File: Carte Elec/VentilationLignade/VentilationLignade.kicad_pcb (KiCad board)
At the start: 2 copper layers, 83 parts, among them P1 RelaisBoard1, P10 SDCard, P11 Codeur Rotatif, P12 Teensy Bottom, P13 EndStops1, P14 Teensy_Haut, P15 EndStops2, P16 Teensy_cote, P17 Retour 12V, P18 Masse_12V, P19 12V1, P2 PUIT_CAN, P20 12V2, P21 12V_1et2, P22 Teensy_Bas, P23 Serial, P24 CHEMINEE, P25 RT_CLK1, P26 RT_CLK2, P3 RelaisBoard2, P4 TEMP_EXT, P5 RelaisBoard3, P6 TEMP_INT, P7 RelaisBoard4, P8 RelaisBoard5, P9 TFT, SW2 BackLight_On/ff, U2 OPTO-TRANSISTOR, U3 OPTO-TRANSISTOR, U4 OPTO-TRANSISTOR, U5 OPTO-TRANSISTOR, U6 OPTO-TRANSISTOR

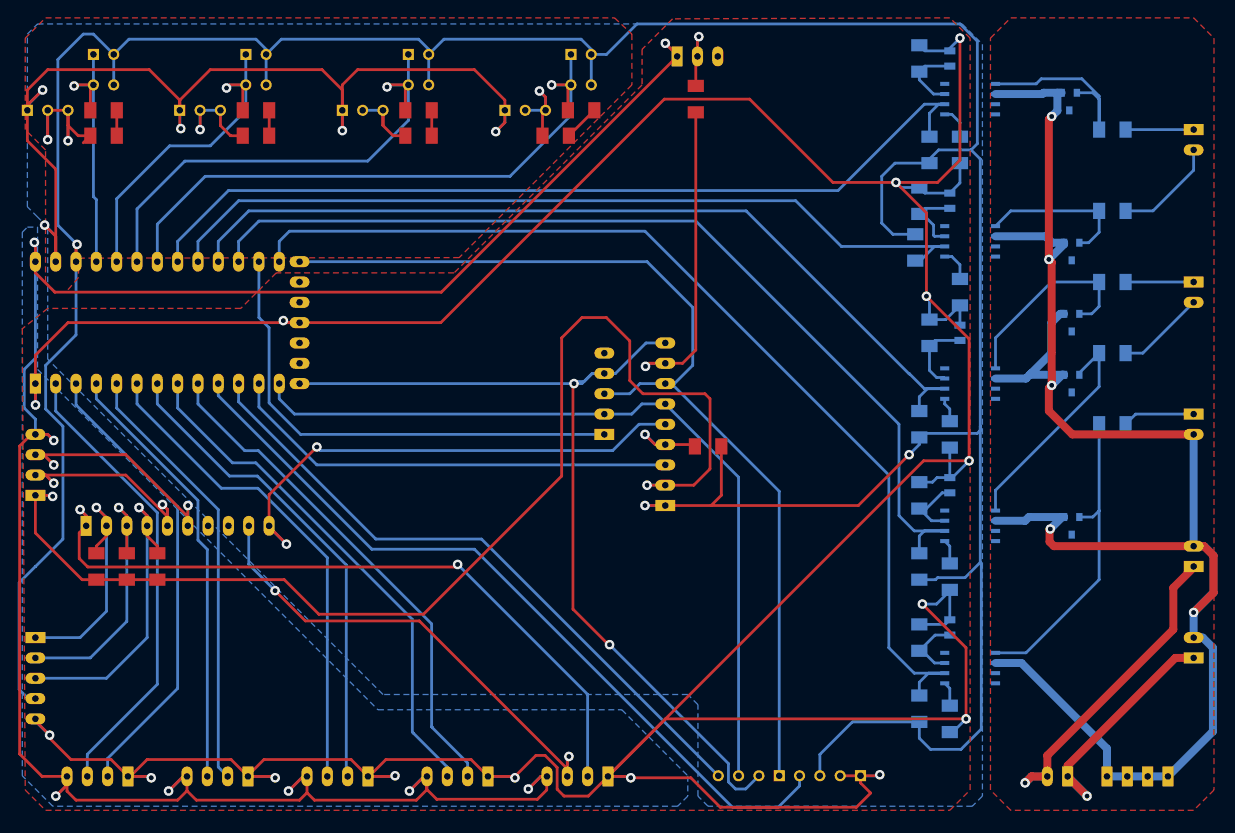
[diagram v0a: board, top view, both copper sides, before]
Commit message: Modif pour ouvrir sur Kicad last version
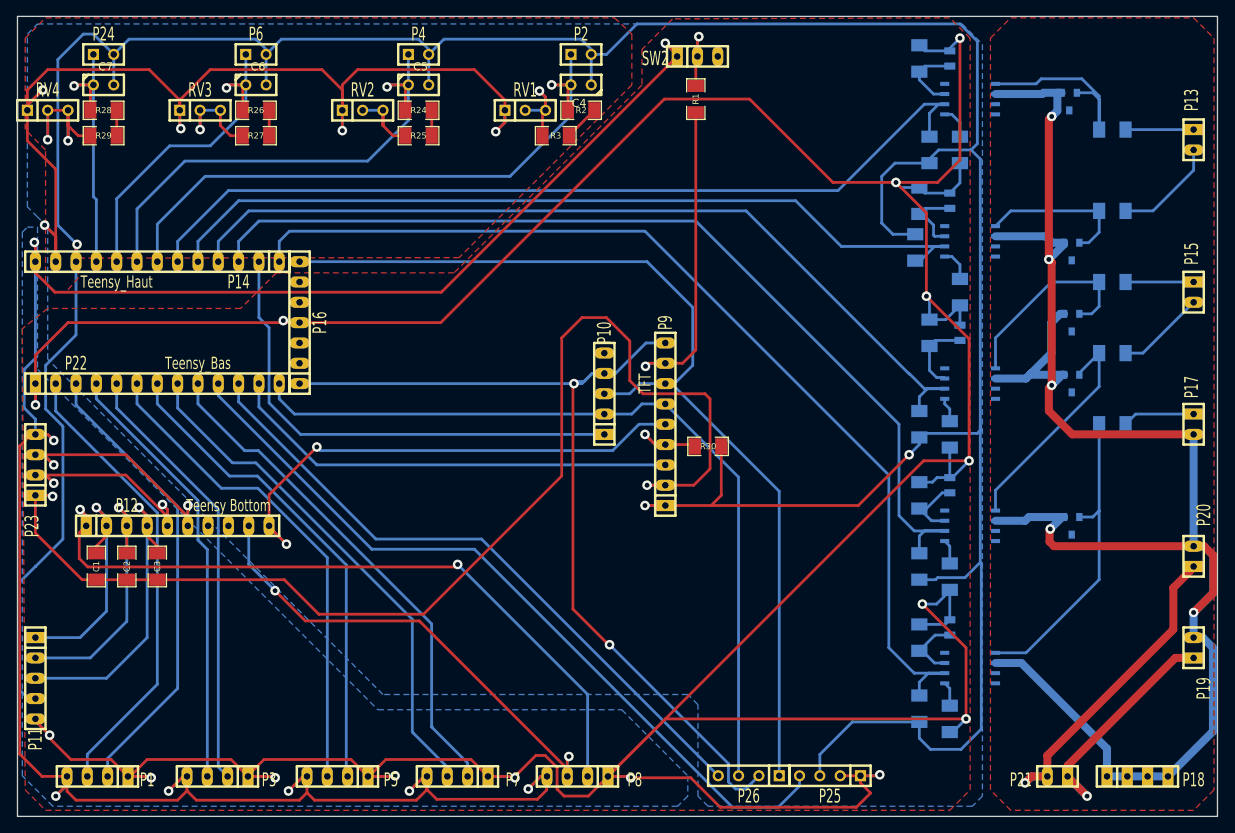
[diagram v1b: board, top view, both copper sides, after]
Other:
- board outline added: 150 x 100 mm

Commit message: Changement des boitiers en cours de reroutage
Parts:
- C4, C5, C6, C7: footprint C1 -> Capacitors_ThroughHole:C_Radial_D8_L11.5_P3.5
- P1, P18, P3, P5, P7, P8: footprint SIL-4 -> Pin_Headers:Pin_Header_Straight_1x04
- P10, P11: footprint SIL-5 -> Pin_Headers:Pin_Header_Straight_1x05
- P12: footprint SIL-10 -> Pin_Headers:Pin_Header_Straight_1x10
- P13, P15, P17, P19, P2, P20, P21, P24, P4, P6: footprint SIL-2 -> Connect:bornier2
- P14, P22: footprint SIL-13 -> Pin_Headers:Pin_Header_Straight_1x13
- P16: footprint SIL-7 -> Pin_Headers:Pin_Header_Straight_1x07
- P9: footprint SIL-9 -> Pin_Headers:Pin_Header_Straight_1x09
- R2, R24, R25, R26, R27, R28, R29, R3: footprint SM1206 -> Resistors_SMD:R_1206_HandSoldering
- RV1, RV2, RV3, RV4: footprint SIL-3 -> Potentiometers:Potentiometer_Bourns_3339S_Angular_ScrewFront
- SW2: footprint SIL-3 -> Pin_Headers:Pin_Header_Straight_1x03
- moved RV3 56.5 mm to (201.9, 105.4)
- moved C4 50.4 mm to (143.5, 115.6), turned to 0 degrees
- moved R2 45.8 mm to (148.6, 121.9)
- moved P2 45.1 mm to (148.6, 105.4), turned to 180 degrees
- moved P6 36.2 mm to (189.2, 105.4), turned to 180 degrees
- moved R27 36.2 mm to (189.2, 115.6), turned to 90 degrees
- moved R3 33.0 mm to (157.5, 115.6), turned to 90 degrees
- moved R26 29.7 mm to (181.6, 121.9)
- moved C6 27.8 mm to (180.3, 115.6)
- moved RV1 26.7 mm to (161.3, 105.4)
- moved P20 18.6 mm to (269.2, 188.0)
- moved RV2 17.3 mm to (181.6, 105.4)
- moved RV4 16.2 mm to (141.0, 105.4)
- moved P22 15.5 mm to (125.2, 147.8), turned to 90 degrees
- moved P14 15.0 mm to (155.7, 132.6), turned to 270 degrees
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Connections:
- C4 pad 1: +3.3V -> TPUIT_AN
- C4 pad 2: TPUIT_AN -> +3.3V
- P10 pad 5: (no net) -> Net-(P10-Pad5)
- P12 pad 7: (no net) -> Net-(P12-Pad7)
- P12 pad 8: (no net) -> Net-(P12-Pad8)
- P13 pad 1: /Optocouplers/END_1_1 -> /Optocouplers/END_1_2
- P13 pad 2: /Optocouplers/END_1_2 -> /Optocouplers/END_1_1
- P14 pad 7: TPUIT_AN -> TINT_AN
- P14 pad 9: TINT_AN -> TPUIT_AN
- P15 pad 1: /Optocouplers/END_2_1 -> /Optocouplers/END_2_2
- P15 pad 2: /Optocouplers/END_2_2 -> /Optocouplers/END_2_1
- P16 pad 2: (no net) -> Net-(P16-Pad2)
- P16 pad 3: (no net) -> Net-(P16-Pad3)
- P16 pad 5: (no net) -> Net-(P16-Pad5)
- P16 pad 6: (no net) -> Net-(P16-Pad6)
- P17 pad 1: /Optocouplers/12V_IN -> GNDPWR
- P17 pad 2: GNDPWR -> /Optocouplers/12V_IN
- P2 pad 1: TPUIT_AN -> +3.3V
- P2 pad 2: +3.3V -> TPUIT_AN
- P24 pad 1: TCHEM_AN -> +3.3V
- P24 pad 2: +3.3V -> TCHEM_AN
- P4 pad 1: TEXT_AN -> +3.3V
- P4 pad 2: +3.3V -> TEXT_AN
- P6 pad 1: TINT_AN -> +3.3V
- P6 pad 2: +3.3V -> TINT_AN
- SW2 pad 3: (no net) -> Net-(SW2-Pad3)
- U2 pad 3: (no net) -> Net-(U2-Pad3)
- U3 pad 3: (no net) -> Net-(U3-Pad3)
- U4 pad 3: (no net) -> Net-(U4-Pad3)
- U5 pad 3: (no net) -> Net-(U5-Pad3)
- U6 pad 3: (no net) -> Net-(U6-Pad3)
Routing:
- net TPUIT_AN: track 77.8 -> 36.7 mm, vias 1 -> 0
- net +3.3V: track 435.3 -> 395.9 mm
- net 12V2: track 40.0 -> 20.9 mm, vias 1 -> 0
- net TINT_AN: track 44.0 -> 62.9 mm, vias 1 -> 0
- net AGND: track 132.8 -> 115.1 mm, vias 5 -> 1
- net GNDPWR: track 221.9 -> 238.3 mm
- net Net-(R29-Pad2): track 24.0 -> 9.21 mm, vias 2 -> 0
- net TEXT_AN: track 62.2 -> 52.0 mm, vias 1 -> 0
- net /Optocouplers/END_1_2: track 13.2 -> 8.24 mm
- net Net-(R24-Pad2): track 3.17 -> 7.42 mm
- net Net-(R26-Pad2): track 3.17 -> 7.42 mm
- net Net-(R2-Pad2): track 4.49 -> 8.69 mm
- net 12V1: track 29.6 -> 33.6 mm, vias 1 -> 0
- net TCHEM_AN: track 34.3 -> 30.5 mm, vias 1 -> 0
- net Net-(R27-Pad2): track 12.6 -> 16.2 mm, vias 1 -> 0
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
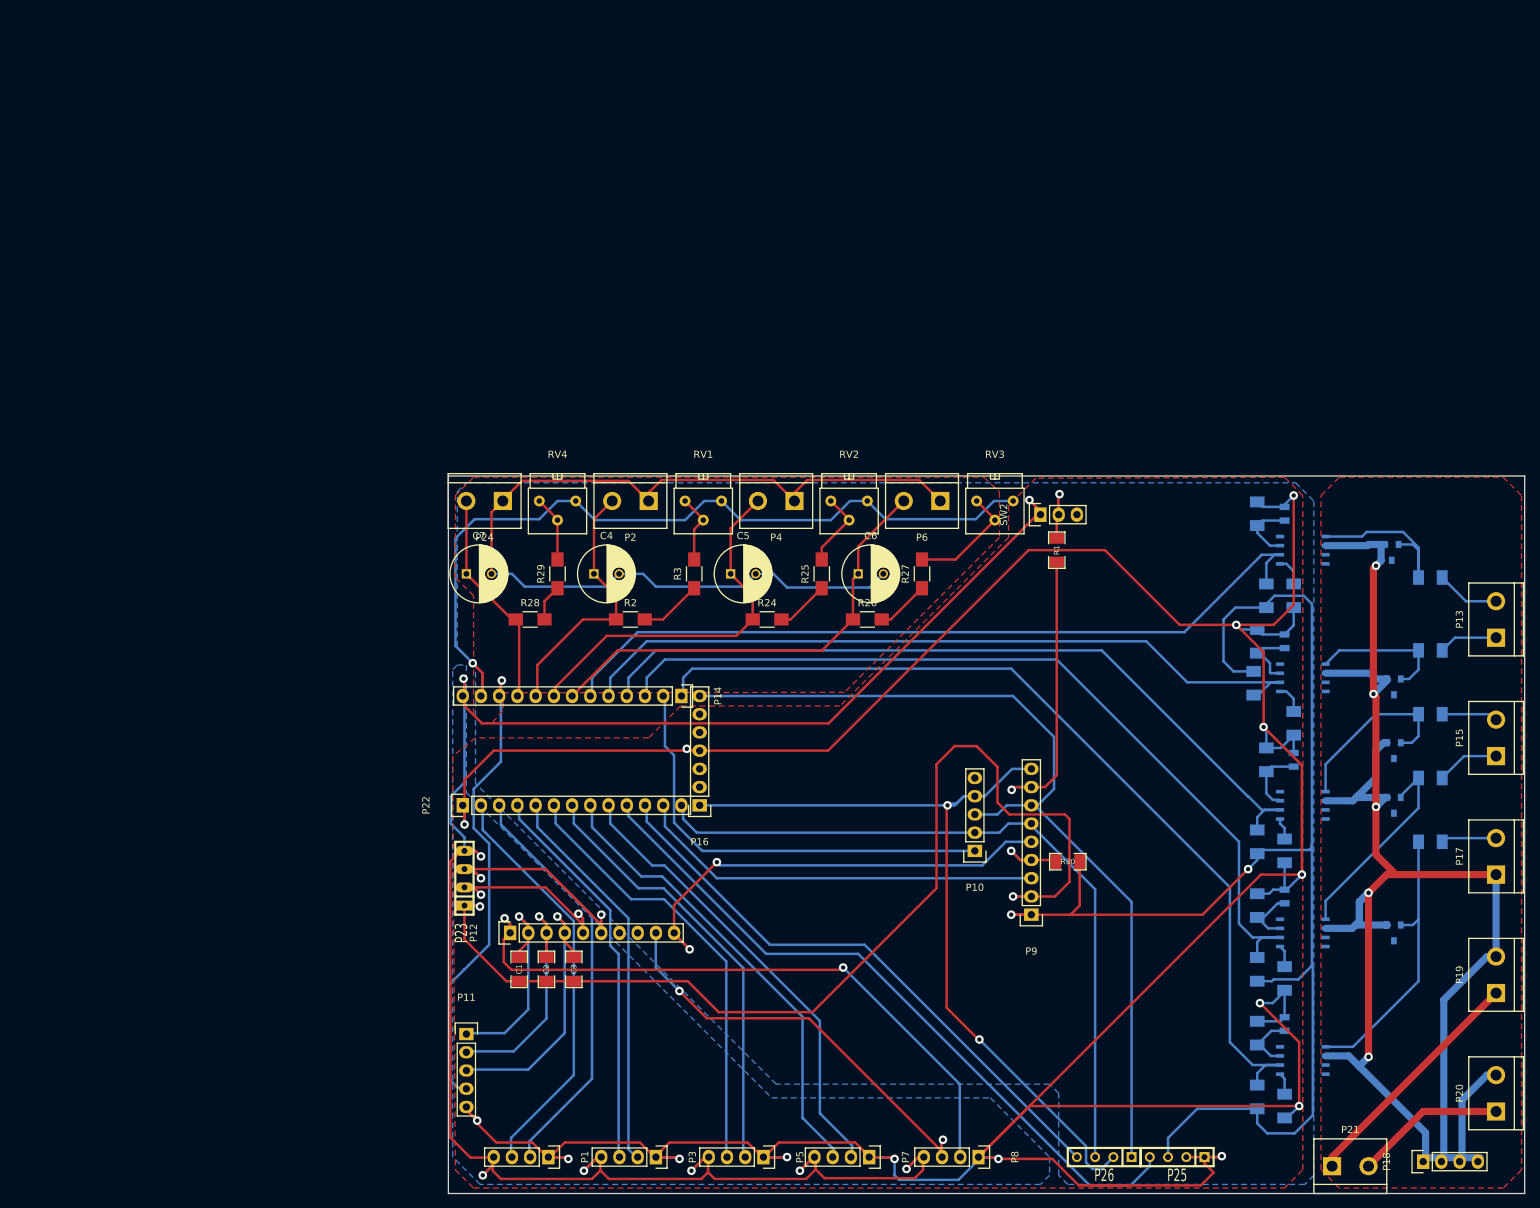
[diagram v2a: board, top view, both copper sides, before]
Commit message: Modif de la carte => Commande SEEED !!!
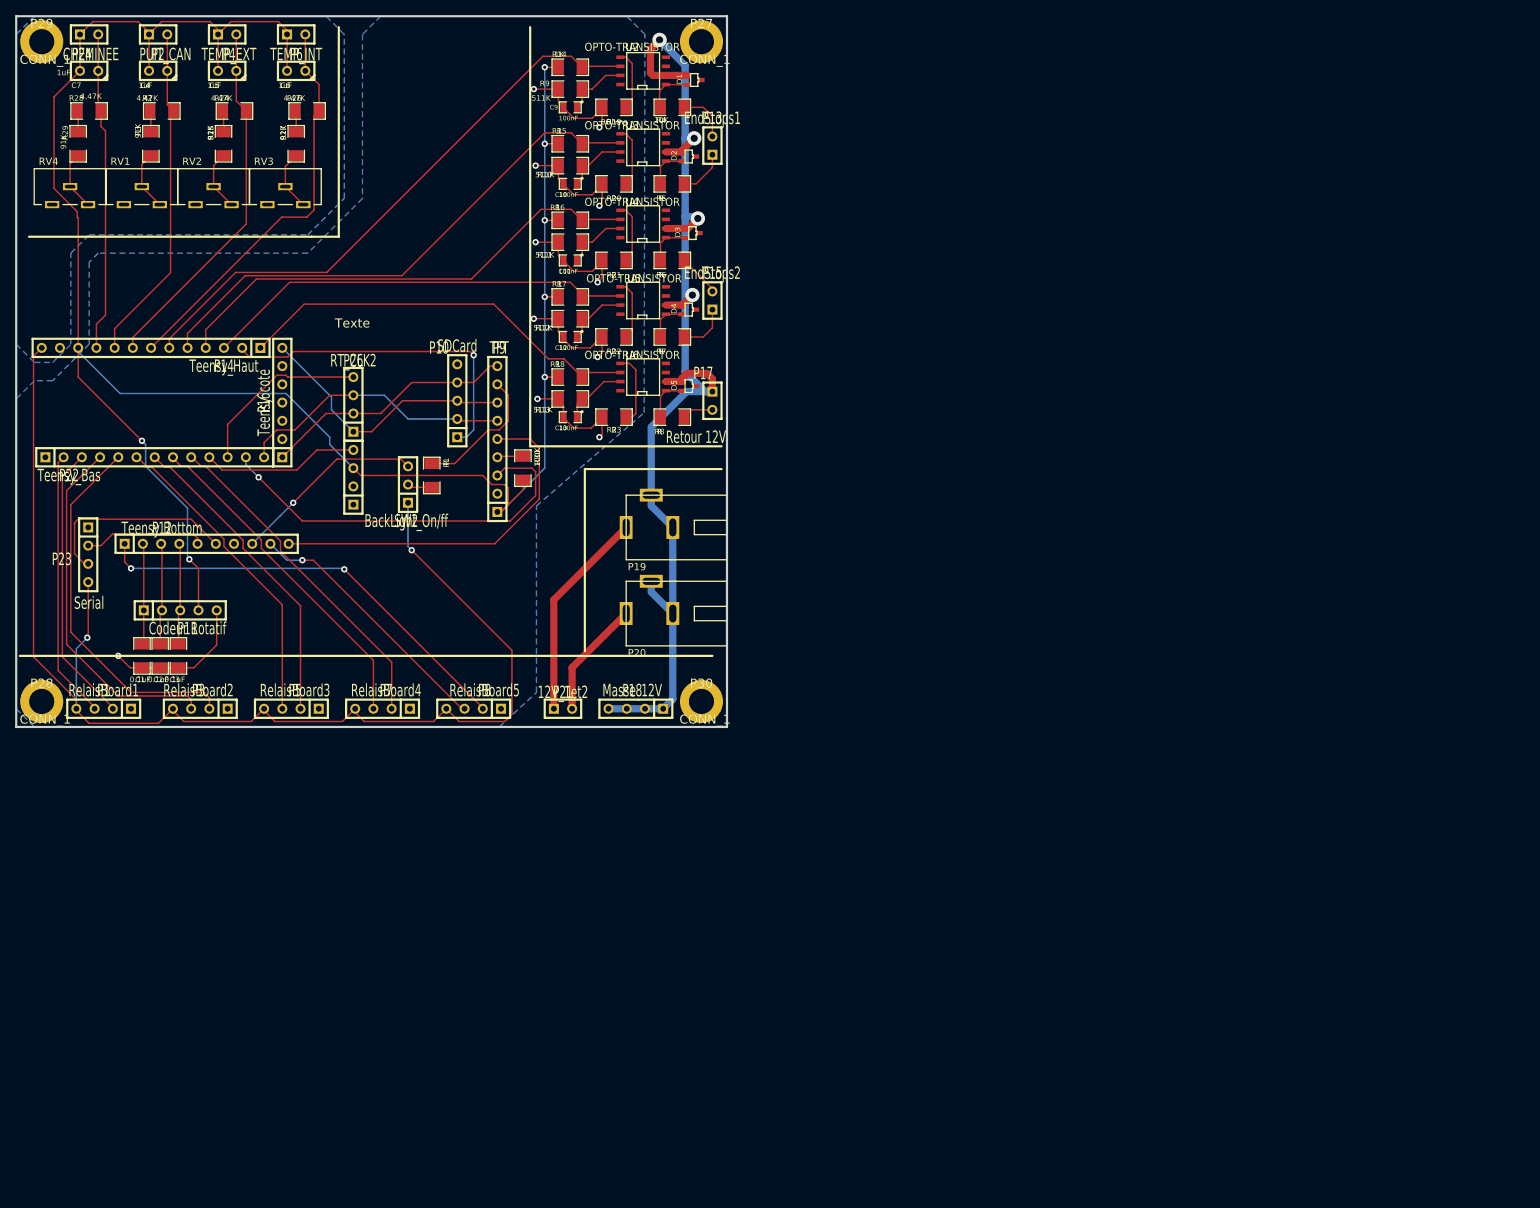
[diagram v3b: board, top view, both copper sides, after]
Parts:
- removed P25: RT_CLK1, SIL-4
- added ?: , SIL-4, F.Cu at (110.0, 102.1)
- added P27: CONN_1, VIS, F.Cu at (158.5, 41.4)
- added P28: CONN_1, VIS, F.Cu at (66.5, 133.3)
- added P29: CONN_1, VIS, F.Cu at (66.5, 41.4)
- added P30: CONN_1, VIS, F.Cu at (158.5, 133.3)
- C10, C11, C12, C13, C9: value C -> 100nF; moved to F.Cu
- C4, C5, C6, C7: footprint Capacitors_ThroughHole:C_Radial_D8_L11.5_P3.5 -> C1
- D1, D2, D3, D4, D5: footprint SOT23 -> SOT323; moved to F.Cu
- P1, P18, P3, P5, P7, P8: footprint Pin_Headers:Pin_Header_Straight_1x04 -> SIL-4
- P10, P11: footprint Pin_Headers:Pin_Header_Straight_1x05 -> SIL-5
- P12: footprint Pin_Headers:Pin_Header_Straight_1x10 -> SIL-10
- P13, P15, P17, P2, P21, P24, P4, P6: footprint Connect:bornier2 -> SIL-2
- P14, P22: footprint Pin_Headers:Pin_Header_Straight_1x13 -> SIL-13
- P16: footprint Pin_Headers:Pin_Header_Straight_1x07 -> SIL-7
- P19: value 12V1 -> CONN_01X03; footprint Connect:bornier2 -> emp:Alim
- P20: value 12V2 -> CONN_01X03; footprint Connect:bornier2 -> emp:Alim
- P9: footprint Pin_Headers:Pin_Header_Straight_1x09 -> SIL-9
- R10, R11, R12, R13, R9: value R -> 511K; moved to F.Cu
- R14: value R -> 1K; moved to F.Cu
- R15, R16, R17, R18, R20, R21, R22, R23, R5, R6, R7, R8, U2, U3, U4, U5, U6: moved to F.Cu
- R19: value R -> 0Ohms; moved to F.Cu
- R2, R24, R25, R26, R27, R28, R29, R3: footprint Resistors_SMD:R_1206_HandSoldering -> SM1206
- R4: value R -> 10K; moved to F.Cu
- RV1, RV2, RV3, RV4: footprint Potentiometers:Potentiometer_Bourns_3339S_Angular_ScrewFront -> emp:Potar
- SW2: footprint Pin_Headers:Pin_Header_Straight_1x03 -> SIL-3
- moved P26 148.2 mm to (110.0, 91.9), turned to 90 degrees
- moved R18 138.7 mm to (140.2, 88.1), turned to 0 degrees
- moved R23 134.0 mm to (146.3, 93.7), turned to 180 degrees
- moved R17 134.0 mm to (140.2, 77.0), turned to 0 degrees
- moved P20 132.8 mm to (154.5, 121.1), turned to 0 degrees
- moved U6 132.4 mm to (150.4, 88.1), turned to 90 degrees
- moved C13 130.6 mm to (140.2, 93.7), turned to 180 degrees
- moved P19 130.6 mm to (154.5, 109.1), turned to 0 degrees
- moved R13 130.3 mm to (140.2, 91.2), turned to 180 degrees
- moved R22 129.3 mm to (146.3, 82.5), turned to 180 degrees
- moved R16 129.1 mm to (140.2, 66.3), turned to 0 degrees
- moved P13 127.6 mm to (160.0, 55.9)
- moved U5 127.4 mm to (150.4, 77.5), turned to 90 degrees
- moved P21 126.9 mm to (139.2, 134.4)
- moved P18 126.6 mm to (149.4, 134.4), turned to 180 degrees
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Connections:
- P12 pad 8: Net-(P12-Pad8) -> TFT_ONOFF
- SW2 pad 3: Net-(SW2-Pad3) -> TFT_ONOFF
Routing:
- net GND: track 689.5 -> 100.5 mm, vias 17 -> 11
- net AGND: track 115.1 -> 0.00 mm, vias 1 -> 0
- net +5V: track 285.4 -> 175.7 mm, vias 8 -> 2
- net +3.3V: track 395.9 -> 293.2 mm, vias 3 -> 7
- net SPI_SCK: track 126.7 -> 37.7 mm
- net SPI_MISO: track 113.6 -> 35.2 mm, vias 2 -> 0
- net GNDPWR: track 238.3 -> 160.9 mm, vias 5 -> 4
- net RTCLK_INTERRUPT: track 97.9 -> 22.0 mm
- net 12V_CHECK: track 127.1 -> 57.2 mm
- net SPI_MOSI: track 101.8 -> 38.8 mm
- net ENDSTOP_2_2: track 120.2 -> 60.2 mm
- net RTCLK_CS: track 81.6 -> 25.0 mm
- net ENDSTOP_2_1: track 109.6 -> 68.0 mm
- net Net-(D5-Pad2): track 39.0 -> 6.23 mm
- net ENDSTOP_1_2: track 104.8 -> 75.0 mm
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- added copper zone on B.Cu, net AGND
- added copper zone on B.Cu, net GND
- removed copper zone on B.Cu, net +3.3V
- removed copper zone on B.Cu, net +5V
- removed copper zone on F.Cu, net AGND
- removed copper zone on F.Cu, net GND
- removed copper zone on F.Cu, net GNDPWR
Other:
- board size 150 x 100 mm -> 99.1 x 99.1 mm
- net class 12V: clearance 0.5 -> 0.4; trace_width 1 -> 1.00076; via_dia 1.2 -> 1.99898; via_drill 0.635 -> 1.00076
- net class Default: clearance 0.35 -> 0.254; trace_width 0.35 -> 0.2032; via_dia 1.2 -> 0.889; via_drill 0.8 -> 0.635
- rule pad_to_mask_clearance: 0 -> 0.254
- rule trace_clearance: 0.35 -> 0.254
- rule trace_min: 0.254 -> 0.2032
- board text added: "12V1"
- board text added: "12V1|V2"
- board text added: "12V2"
- board text added: "ByPass1"
- board text added: "ByPass2"
- board text added: "Cave|Chem."
- board text added: "Cheminée"
- board text added: "Codeur Rotatif"
- board text added: "Extérieur"
- board text added: "FdC1"
- board text added: "FdC2"
- board text added: "Intérieur"
- board text added: "Masse 12V"
- board text added: "OptoCoupleurs"
- board text added: "Prises de Température"
- board text added: "Puit Can."
- board text added: "RT Clock"
- board text added: "Relais"
- board text added: "Ret.12V"
- board text added: "SDCard"
- board text added: "Screen SW"
- board text added: "Serial"
- board text added: "TFT"
- board text added: "Teensy 3.1/3.2"
- board text added: "Teensy Dessous"
- board text added: "Texte"
- board text added: "Transfos 12V"
- board text added: "V1|VMC"
- board text added: "V2|SelV"
